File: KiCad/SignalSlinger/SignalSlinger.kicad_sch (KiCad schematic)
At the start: 63 parts, among them J101 Conn_01x02, J102 Conn_01x03, J103 Conn_01x02, J104 Conn_01x02, J105 Conn_01x04, J106 Conn_01x02, J107 DB9 Female, J109 SolderJumper_2_Bridged, P101 ISP/PDI, Q101 BSS84W-7-F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

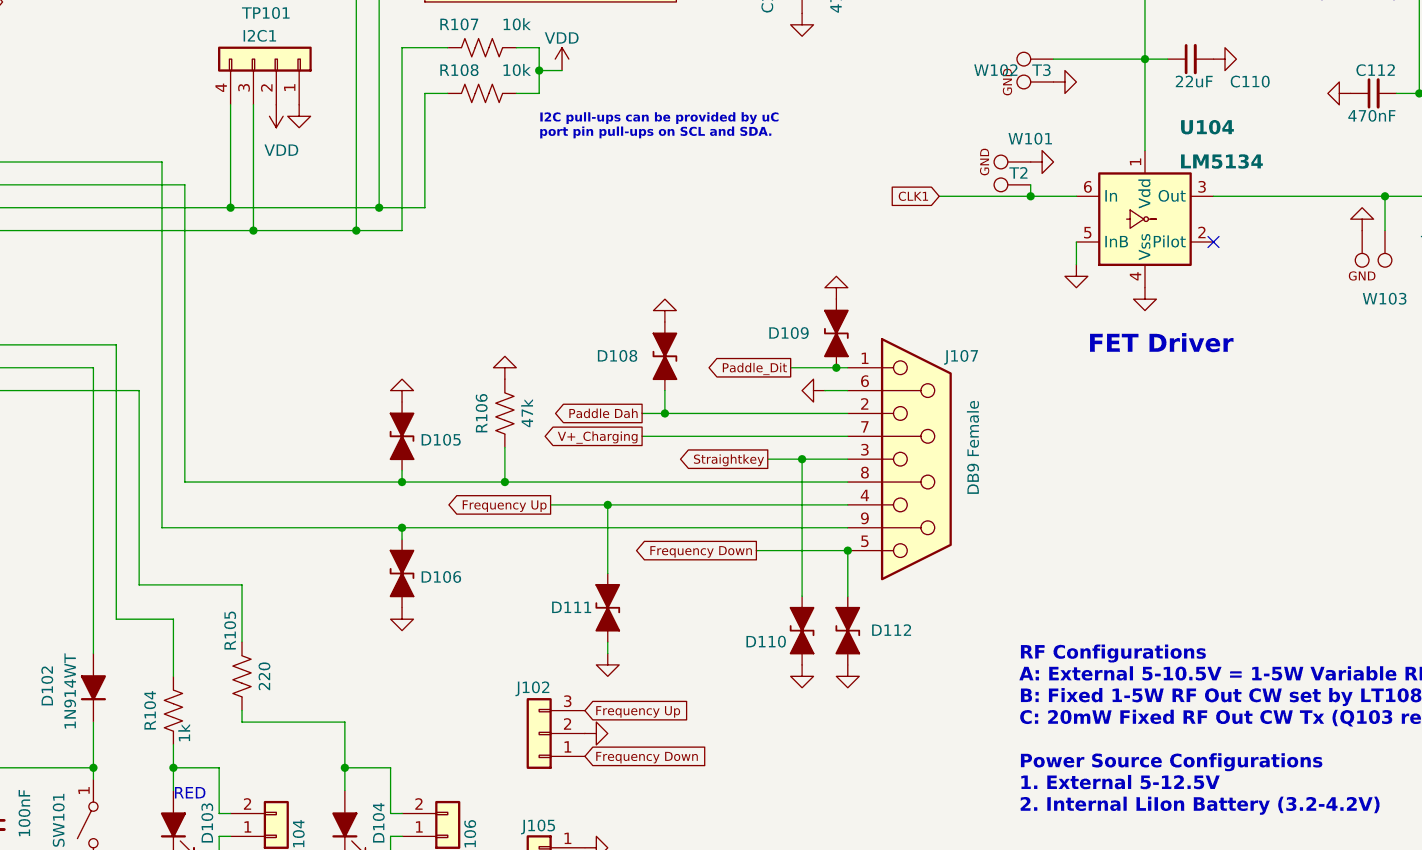
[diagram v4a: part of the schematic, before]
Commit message: DB9 Pinout Updates
o Updated schematic (Rev 2.0)
o Updated PCB
o Updated Gerbers
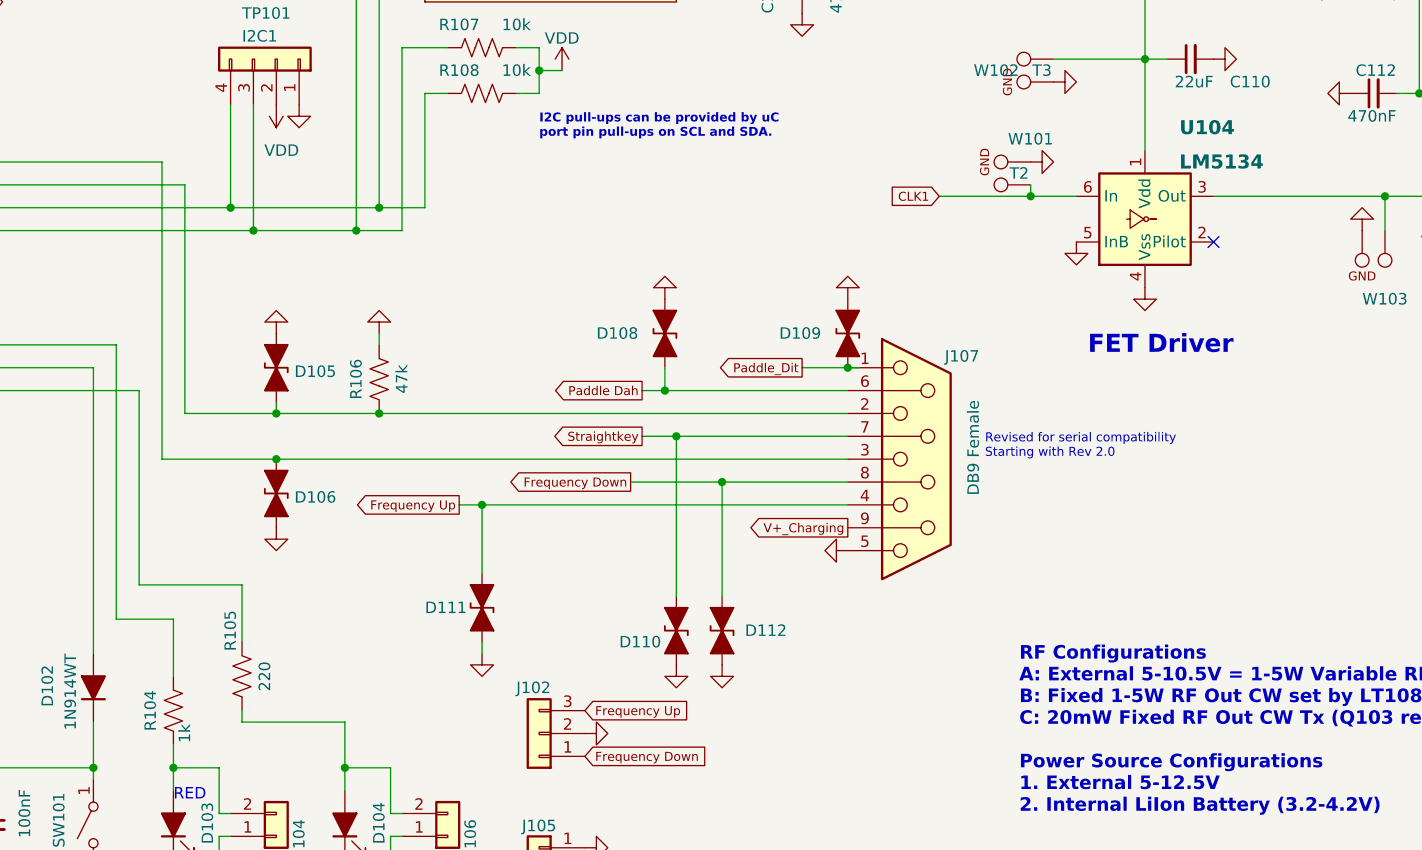
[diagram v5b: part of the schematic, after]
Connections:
- net Frequency Down: now also J107.8; no longer J107.5
- net GND: now also J107.5; no longer J107.6
- net Paddle Dah: now also J107.6; no longer J107.2
- net Straightkey: now also J107.7; no longer J107.3
- net V+_Charging: now also J107.9; no longer J107.7
- net at D105.2 (A2), R106.1, U101.3 (PC1/RxD1): now also J107.2; no longer J107.8
- net at D106.1 (A1), U101.2 (PC0/TxD1): now also J107.3; no longer J107.9
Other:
- note added: "Revised for serial compatibility Starting with Rev 2.0"
- moved on the sheet: D105, D106, D108, D109, D110, D111, D112, R106

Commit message: KiCad Updates
Updated schematic and PCB.
Added diodes to support USB powering the processor and replacing J202
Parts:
- D113, D114: value 1N914WT -> 1N4001; footprint Diode_SMD:D_SOD-523 -> Diode_SMD:D_SOD-123F; Digi-Key Part No. (none) -> HS1AFLCT-ND; Link (none) -> https://www.digikey.com/en/products/detail/taiwan-semicondu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; Manufacturer (none) -> Taiwan Semiconductor Corporation; Manufacturer PN (none) -> HS1AFL
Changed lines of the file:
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@@
     (title "SignalSlinger")
     (date "2023-11-21")
-    (rev "2.0")
+    (rev "2.1")
   )
   (junction (at 154.94 81.28) (diameter 0) (color 0 0 0 0)
@@
       (effects (font (size 1.27 1.27)) (justify left))
     )
-    (property "Value" "1N914WT" (id 1) (at 247.142 52.5022 90)
+    (property "Value" "1N4001" (id 1) (at 247.142 52.5022 90)
       (effects (font (size 1.27 1.27)) (justify left) hide)
     )
-    (property "Footprint" "Diode_SMD:D_SOD-523" (id 2) (at 240.665 50.8 0)
+    (property "Footprint" "Diode_SMD:D_SOD-123F" (id 2) (at 240.665 50.8 0)
       (effects (font (size 1.27 1.27)) hide)
     )
-    (property "Datasheet" "http://www.mouser.com/ds/2/149/1N4148WT-461550.pdf" (id 3) (at 245.11 50.8 0)
+    (property "Datasheet" "" (id 3) (at 245.11 50.8 0)
+      (effects (font (size 1.27 1.27)) hide)
+    )
+    (property "Digi-Key Part No." "HS1AFLCT-ND" (id 4) (at 245.11 50.8 0)
+      (effects (font (size 1.27 1.27)) hide)
+    )
+    (property "Link" "https://www.digikey.com/en/products/detail/taiwan-semiconductor-corporation/HS1AFL/9602851?s=N4IgTCBcDaIBIGUCMBBAYgGQMIBUC0AcgCIgC6AvkA" (id 5) (at 245.11 50.8 0)
+      (effects (font (size 1.27 1.27)) hide)
+    )
+    (property "Manufacturer" "Taiwan Semiconductor Corporation" (id 6) (at 245.11 50.8 0)
+      (effects (font (size 1.27 1.27)) hide)
+    )
+    (property "Manufacturer PN" "HS1AFL" (id 7) (at 245.11 50.8 0)
+      (effects (font (size 1.27 1.27)) hide)
+    )
+    (property "Description" "DIODE GEN PURP 50V 1A SOD123F" (id 8) (at 245.11 50.8 0)
       (effects (font (size 1.27 1.27)) hide)
     )
@@
       (effects (font (size 1.27 1.27)) (justify left))
     )
-    (property "Value" "1N914WT" (id 1) (at 262.0522 60.198 90)
+    (property "Value" "1N4001" (id 1) (at 262.0522 60.198 90)
       (effects (font (size 1.27 1.27)) (justify left) hide)
     )
-    (property "Footprint" "Diode_SMD:D_SOD-523" (id 2) (at 260.35 66.675 0)
+    (property "Footprint" "Diode_SMD:D_SOD-123F" (id 2) (at 260.35 66.675 0)
+      (effects (font (size 1.27 1.27)) hide)
+    )
+    (property "Datasheet" "" (id 3) (at 260.35 62.23 0)
       (effects (font (size 1.27 1.27)) hide)
     )
-    (property "Datasheet" "http://www.mouser.com/ds/2/149/1N4148WT-461550.pdf" (id 3) (at 260.35 62.23 0)
+    (property "Digi-Key Part No." "HS1AFLCT-ND" (id 4) (at 260.35 62.23 0)
+      (effects (font (size 1.27 1.27)) hide)
+    )
+    (property "Link" "https://www.digikey.com/en/products/detail/taiwan-semiconductor-corporation/HS1AFL/9602851?s=N4IgTCBcDaIBIGUCMBBAYgGQMIBUC0AcgCIgC6AvkA" (id 5) (at 260.35 62.23 0)
+      (effects (font (size 1.27 1.27)) hide)
+    )
+    (property "Manufacturer" "Taiwan Semiconductor Corporation" (id 6) (at 260.35 62.23 0)
+      (effects (font (size 1.27 1.27)) hide)
+    )
+    (property "Manufacturer PN" "HS1AFL" (id 7) (at 260.35 62.23 0)
+      (effects (font (size 1.27 1.27)) hide)
+    )
+    (property "Description" "DIODE GEN PURP 50V 1A SOD123F" (id 8) (at 260.35 62.23 0)
       (effects (font (size 1.27 1.27)) hide)
     )
@@
     )
     (path "/76a10c0b-6cb7-464f-9327-60d8d92cce59"
-      (reference "D113") (unit 1) (value "1N914WT") (footprint "Diode_SMD:D_SOD-523")
+      (reference "D113") (unit 1) (value "1N4001") (footprint "Diode_SMD:D_SOD-123F")
     )
     (path "/c8421619-bfcc-4db9-9d95-17391592de97"
-      (reference "D114") (unit 1) (value "1N914WT") (footprint "Diode_SMD:D_SOD-523")
+      (reference "D114") (unit 1) (value "1N4001") (footprint "Diode_SMD:D_SOD-123F")
     )
     (path "/b7c888bf-e50e-45b8-8886-9bc5abf637fe/33cd1e3c-0750-4827-bb26-b547e05a9d0c"
@@
       (reference "D202") (unit 1) (value "B330A Schottky Diode") (footprint "Diode_SMD:D_SMA")
     )
+    (path "/b7c888bf-e50e-45b8-8886-9bc5abf637fe/e20bf944-d393-4fd1-97b5-6fd7f7604c33"
+      (reference "D203") (unit 1) (value "Schottky Diode") (footprint "Diode_SMD:D_SOD-123")
+    )
+    (path "/b7c888bf-e50e-45b8-8886-9bc5abf637fe/62e6bdff-cfbb-4ca4-8d2b-9934a718df37"
+      (reference "D204") (unit 1) (value "Schottky Diode") (footprint "Diode_SMD:D_SOD-123")
+    )
     (path "/b7c888bf-e50e-45b8-8886-9bc5abf637fe/3f758ec9-95f3-4acf-8bdb-6d3c6615ff72"
       (reference "F201") (unit 1) (value "1.1A") (footprint "Fuse:Fuse_1812_4532Metric")
@@
       (reference "J201") (unit 1) (value "Barrel_Jack_Switch") (footprint "Connector_BarrelJack:BarrelJack_CUI_PJ-036AH-SMT_Horizontal")
     )
-    (path "/b7c888bf-e50e-45b8-8886-9bc5abf637fe/ae8ffd1e-be1d-4f41-b4e2-0842fe0cb899"
-      (reference "J202") (unit 1) (value "SolderJumper_3_Bridged12") (footprint "Jumper:SolderJumper-3_P1.3mm_Bridged12_RoundedPad1.0x1.5mm_NumberLabels")
-    )
     (path "/b7c888bf-e50e-45b8-8886-9bc5abf637fe/24613239-e381-4dca-9f8d-2951032dcaef"
-      (reference "J203") (unit 1) (value "External Power Source") (footprint "Connector_PinHeader_2.54mm:PinHeader_1x02_P2.54mm_Vertical")
+      (reference "J203") (unit 1) (value "External Fan Power") (footprint "Connector_PinHeader_2.54mm:PinHeader_1x02_P2.54mm_Vertical")
     )
     (path "/b7c888bf-e50e-45b8-8886-9bc5abf637fe/fbf68feb-d68b-4b02-93fe-c4e54200e911"

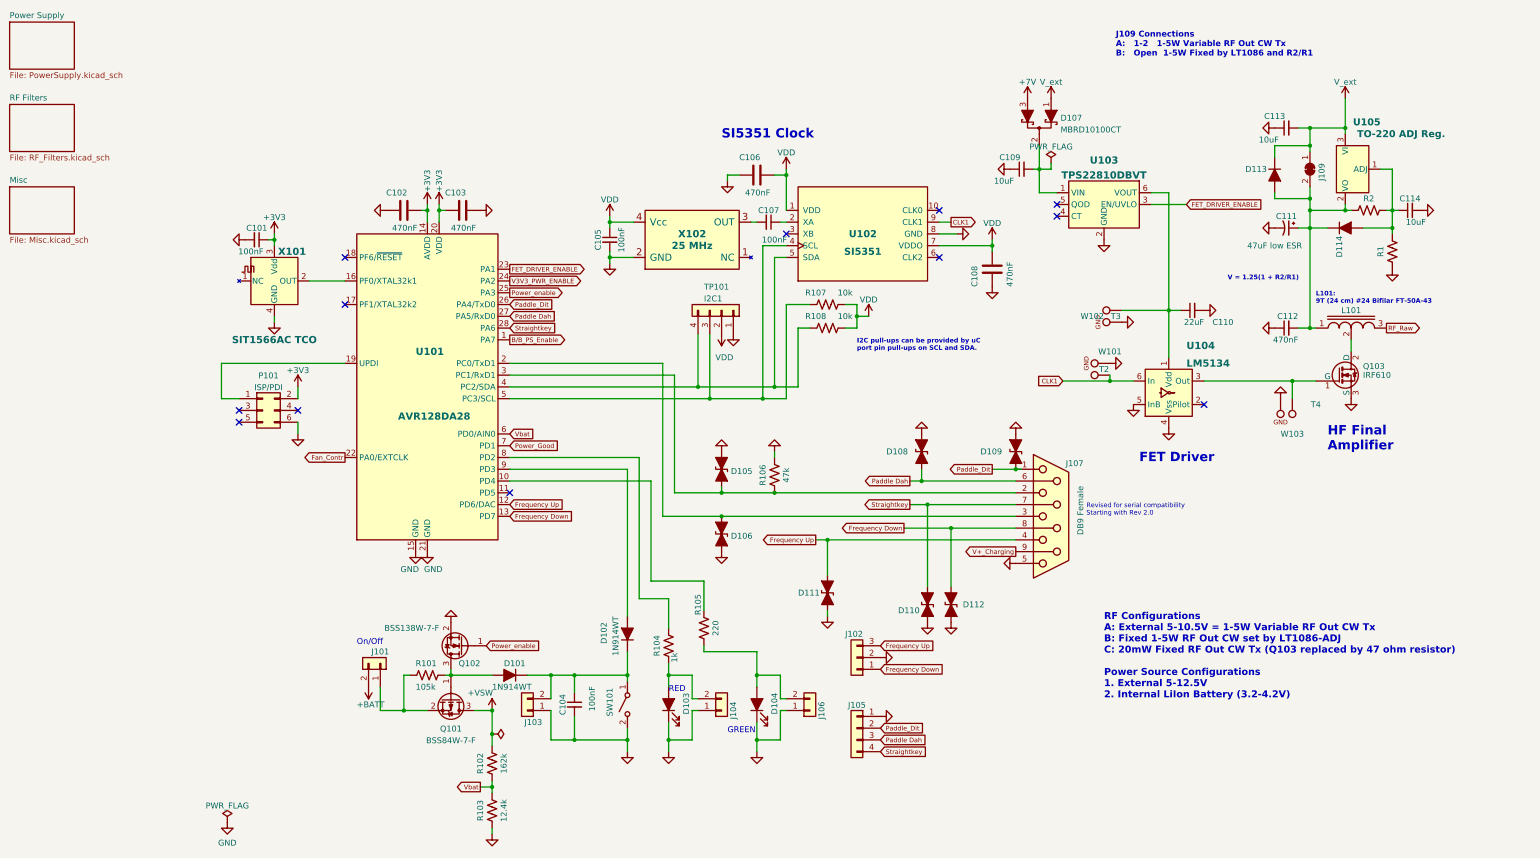
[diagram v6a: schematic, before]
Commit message: Schematic & PCB Updates
o Improvements to DC power routing
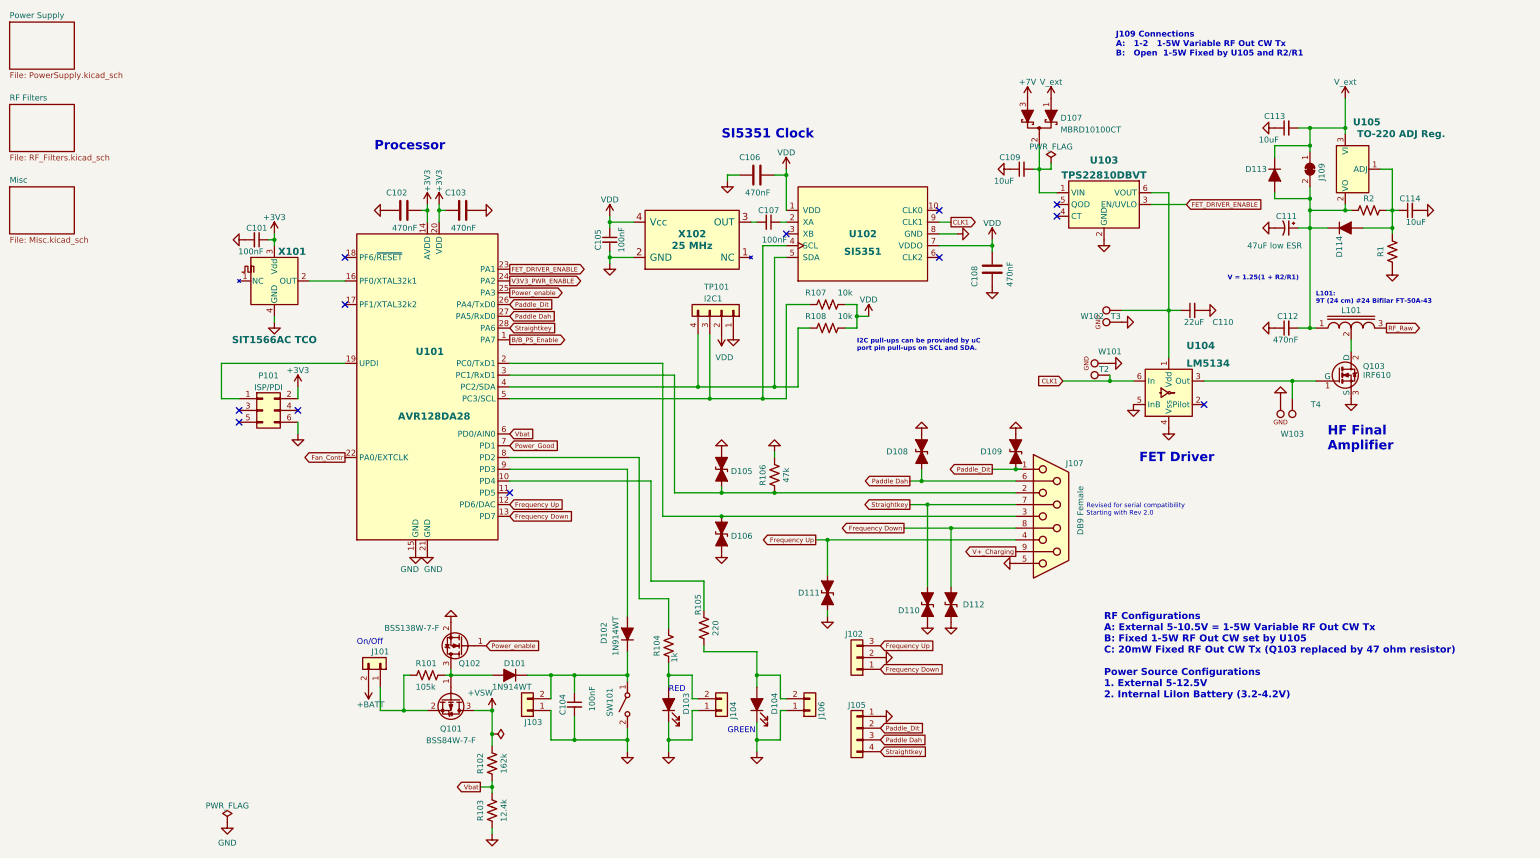
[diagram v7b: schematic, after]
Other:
- note added: "J109 Connections A: 1-2 1-5W Variable RF Out CW Tx B: Open 1-5W Fixed by U105 and R2/R1"
- note added: "Processor"
- note added: "RF Configurations A: External 5-10.5V = 1-5W Variable RF Out CW Tx B: Fixed 1-5W RF Out CW set by U105 C: 20mW Fixed RF Out CW Tx (Q103 replaced by 47 ohm resistor) Power Source Configurations 1. External 5-12.5V 2. Internal LiIon Battery (3.2-4.2V)"
- note removed: "J109 Connections A: 1-2 1-5W Variable RF Out CW Tx B: Open 1-5W Fixed by LT1086 and R2/R1"
- note removed: "RF Configurations A: External 5-10.5V = 1-5W Variable RF Out CW Tx B: Fixed 1-5W RF Out CW set by LT1086-ADJ C: 20mW Fixed RF Out CW Tx (Q103 replaced by 47 ohm resistor) Power Source Configurations 1. External 5-12.5V 2. Internal LiIon Battery (3.2-4.2V)"
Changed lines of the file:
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@@
   (title_block
     (title "SignalSlinger")
-    (date "2023-11-21")
-    (rev "2.1")
+    (date "2023-12-10")
+    (rev "2.2")
   )
   (junction (at 154.94 81.28) (diameter 0) (color 0 0 0 0)
@@
     (effects (font (size 1 1)) (justify left bottom))
   )
-  (text "J109 Connections\nA:   1-2   1-5W Variable RF Out CW Tx\nB:   Open  1-5W Fixed by LT1086 and R2/R1"
+  (text "J109 Connections\nA:   1-2   1-5W Variable RF Out CW Tx\nB:   Open  1-5W Fixed by U105 and R2/R1"
     (at 210.82 25.4 0)
     (effects (font (size 1.27 1.27) (thickness 0.254) bold) (justify left bottom))
@@
     (effects (font (size 2.0066 2.0066) (thickness 0.4013) bold) (justify left bottom))
   )
-  (text "RF Configurations\nA: External 5-10.5V = 1-5W Variable RF Out CW Tx\nB: Fixed 1-5W RF Out CW set by LT1086-ADJ\nC: 20mW Fixed RF Out CW Tx (Q103 replaced by 47 ohm resistor)\n\nPower Source Configurations\n1. External 5-12.5V\n2. Internal LiIon Battery (3.2-4.2V)\n\n"
+  (text "RF Configurations\nA: External 5-10.5V = 1-5W Variable RF Out CW Tx\nB: Fixed 1-5W RF Out CW set by U105\nC: 20mW Fixed RF Out CW Tx (Q103 replaced by 47 ohm resistor)\n\nPower Source Configurations\n1. External 5-12.5V\n2. Internal LiIon Battery (3.2-4.2V)\n\n"
     (at 208.28 166.37 0)
     (effects (font (size 1.5 1.5) (thickness 0.3) bold) (justify left bottom))
@@
     (effects (font (size 0.9906 0.9906) (thickness 0.1981) bold) (justify left bottom))
   )
+  (text "Processor" (at 50.8 45.72 0)
+    (effects (font (size 2.0066 2.0066) (thickness 0.4013) bold) (justify left bottom))
+  )
   (text "RED" (at 114.3 162.56 0)
     (effects (font (size 1.27 1.27)) (justify left bottom))
@@
     )
     (path "/b7c888bf-e50e-45b8-8886-9bc5abf637fe/67c41640-a5e7-4fd7-a17b-9c7fc94c4026"
-      (reference "D202") (unit 1) (value "B330A Schottky Diode") (footprint "Diode_SMD:D_SMA")
+      (reference "D202") (unit 1) (value "B330A Schottky Diode") (footprint "Diode_SMD:D_SMB")
     )
     (path "/b7c888bf-e50e-45b8-8886-9bc5abf637fe/e20bf944-d393-4fd1-97b5-6fd7f7604c33"
@@
       (reference "D204") (unit 1) (value "Schottky Diode") (footprint "Diode_SMD:D_SOD-123")
     )
+    (path "/b7c888bf-e50e-45b8-8886-9bc5abf637fe/1e9eae5c-a7ca-4c5b-a119-8ee2c6cbc7b0"
+      (reference "D205") (unit 1) (value "Schottky Diode") (footprint "Diode_SMD:D_SOD-123")
+    )
     (path "/b7c888bf-e50e-45b8-8886-9bc5abf637fe/3f758ec9-95f3-4acf-8bdb-6d3c6615ff72"

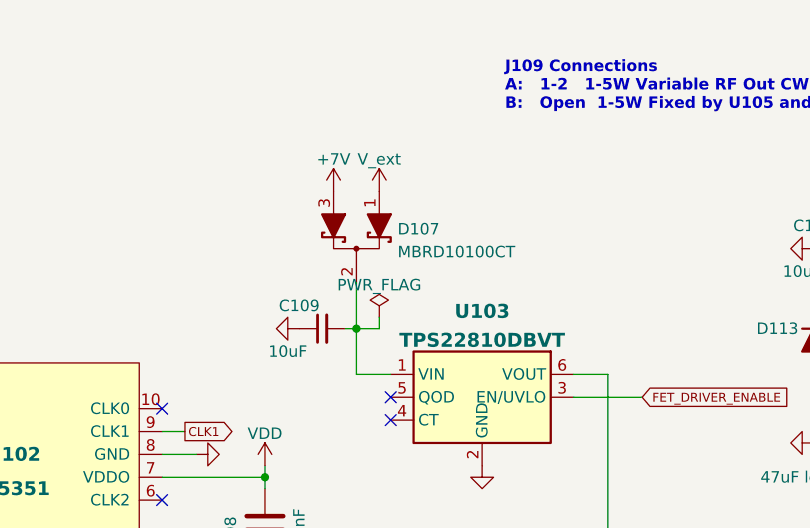
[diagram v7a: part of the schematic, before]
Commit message: Schematic Update
o Power routing improvement
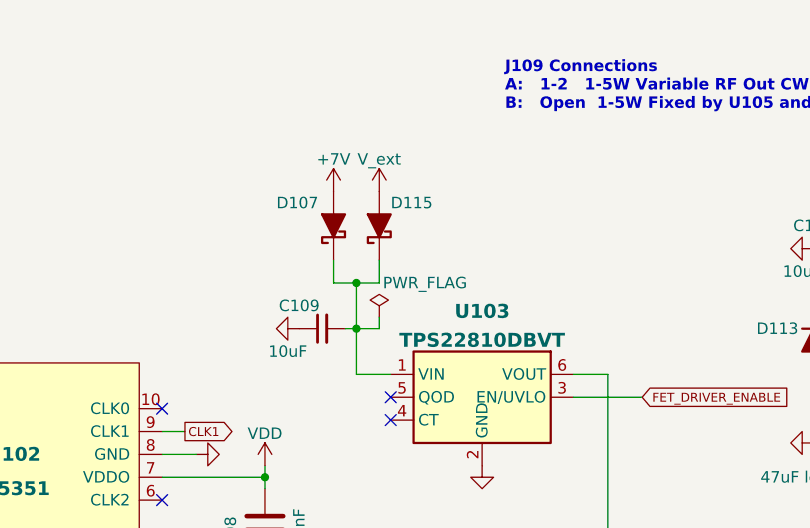
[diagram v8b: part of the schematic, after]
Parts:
- removed D107: MBRD10100CT, Package_TO_SOT_SMD:TO-252-2, symbol Device:D_Schottky_Dual_CommonCathode_AKA_Parallel
- added D107, D115: Schottky Diode, Diode_SMD:D_SOD-123FL, symbol Device:D_Schottky_Filled
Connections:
- net +7V: now also D107.2 (A)
- net V_ext: now also D115.2 (A)
- net at C109.2, U103.1 (VIN): now also D107.1 (K), D115.1 (K)
